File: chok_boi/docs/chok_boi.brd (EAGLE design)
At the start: 160 x 100 mm, 94 parts, among them U1 MPU-6000, U2 DRV8835

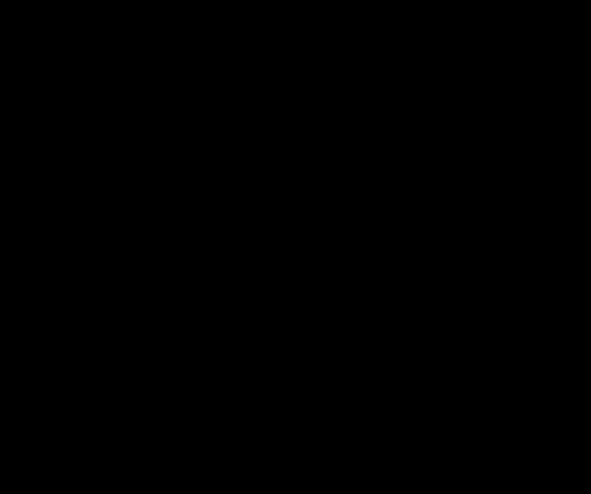
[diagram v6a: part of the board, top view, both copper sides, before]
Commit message: Add bypass caps to DRV8835
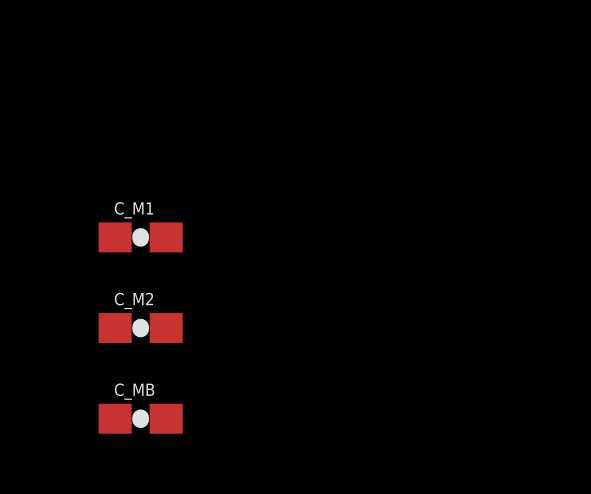
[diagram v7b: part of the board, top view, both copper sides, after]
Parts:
- added C_M1, C_M2: 0.1uF, SparkFun:0603-CAP
- added C_MB: 100uF, SparkFun:0603-CAP
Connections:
- net 3.3V: now also C_M1.2
- net BATTERY: now also C_M2.2, C_MB.2
- net MGND: now also C_M1.1, C_M2.1, C_MB.1
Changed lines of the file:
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@@
 <attribute name="PROD_ID" value="IC-13342" x="17.7038" y="37.0078" size="1.778" layer="27" display="off"/>
 </element>
+<element name="C_M1" library="SparkFun" package="0603-CAP" value="0.1uF" x="-4.5212" y="-234.3658"/>
+<element name="C_M2" library="SparkFun" package="0603-CAP" value="0.1uF" x="-4.5212" y="-237.3884"/>
+<element name="C_MB" library="SparkFun" package="0603-CAP" value="100uF" x="-4.5212" y="-240.411"/>
 </elements>
 <signals>
@@
 <wire x1="16.1846" y1="42.40075625" x2="16.1846" y2="40.9776" width="1.524" layer="1"/>
 <contactref element="U2" pad="1"/>
-<wire x1="17.1314" y1="55.3466" x2="9.906" y2="69.596" width="0" layer="19" extent="1-1"/>
-<wire x1="16.4084" y1="45.1866" x2="17.1314" y2="55.3466" width="0" layer="19" extent="1-1"/>
+<contactref element="C_M2" pad="2"/>
+<contactref element="C_MB" pad="2"/>
+<wire x1="-3.6712" y1="-237.3884" x2="-3.6712" y2="-240.411" width="0" layer="19" extent="1-1"/>
+<wire x1="16.4538" y1="35.9578" x2="-3.6712" y2="-237.3884" width="0" layer="19" extent="1-1"/>
+<wire x1="16.1846" y1="40.9776" x2="16.4538" y2="35.9578" width="0" layer="19" extent="1-1"/>
 <wire x1="6.731" y1="39.276" x2="8.57660625" y2="40.3606" width="0" layer="19" extent="1-16"/>
 <wire x1="5.461" y1="39.276" x2="6.731" y2="39.276" width="0" layer="19" extent="1-1"/>
-<wire x1="16.4538" y1="35.9578" x2="5.461" y2="39.276" width="0" layer="19" extent="1-1"/>
+<wire x1="17.1314" y1="55.3466" x2="16.4084" y2="45.1866" width="0" layer="19" extent="1-1"/>
+<wire x1="9.906" y1="69.596" x2="17.1314" y2="55.3466" width="0" layer="19" extent="1-1"/>
 </signal>
 <signal name="5V">
@@
 <wire x1="3.81" y1="27.6606" x2="3.7338" y2="27.7368" width="1.524" layer="1"/>
 <contactref element="U2" pad="12"/>
-<wire x1="2.8448" y1="11.938" x2="16.4538" y2="38.0578" width="0" layer="19" extent="1-1"/>
+<contactref element="C_M1" pad="2"/>
+<wire x1="2.8448" y1="11.938" x2="-3.6712" y2="-234.3658" width="0" layer="19" extent="1-1"/>
 <wire x1="10.0124" y1="27.5336" x2="5.908" y2="27.766" width="0" layer="19" extent="1-1"/>
 <wire x1="10.2244" y1="27.5336" x2="10.0124" y2="27.5336" width="0" layer="19" extent="1-1"/>
-<wire x1="43.6254" y1="30.9372" x2="10.2244" y2="27.5336" width="0" layer="19" extent="1-1"/>
-<wire x1="43.7016" y1="33.3502" x2="43.6254" y2="30.9372" width="0" layer="19" extent="1-1"/>
+<wire x1="16.4538" y1="38.0578" x2="10.2244" y2="27.5336" width="0" layer="19" extent="1-1"/>
+<wire x1="43.7016" y1="33.3502" x2="16.4538" y2="38.0578" width="0" layer="19" extent="1-1"/>
+<wire x1="43.6254" y1="30.9372" x2="43.7016" y2="33.3502" width="0" layer="19" extent="1-1"/>
 <wire x1="48.221" y1="33.0816" x2="43.7016" y2="33.3502" width="0" layer="19" extent="1-1"/>
 <wire x1="50.221" y1="31.0816" x2="48.221" y2="33.0816" width="0" layer="19" extent="1-1"/>
@@
 <contactref element="U2" pad="6"/>
 <contactref element="U2" pad="PAD"/>
+<contactref element="C_M1" pad="1"/>
+<contactref element="C_M2" pad="1"/>
+<contactref element="C_MB" pad="1"/>
+<wire x1="-5.3712" y1="-237.3884" x2="-5.3712" y2="-240.411" width="0" layer="19" extent="1-1"/>
+<wire x1="-5.3712" y1="-234.3658" x2="-5.3712" y2="-237.3884" width="0" layer="19" extent="1-1"/>
+<wire x1="18.9538" y1="35.9578" x2="-5.3712" y2="-234.3658" width="0" layer="19" extent="1-1"/>
 <wire x1="17.7038" y1="37.0078" x2="18.9538" y2="35.9578" width="0" layer="19" extent="1-1"/>
 <wire x1="19.939" y1="43.67940625" x2="17.7038" y2="37.0078" width="0" layer="19" extent="1-1"/>

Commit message: Add cell outline
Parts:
- moved LEFT_FRONT_EMITTER 29.6 mm to (60.0, 69.0)
- moved U$18 27.7 mm to (77.0, 42.0)
- moved REC_LF 27.2 mm to (64.0, 63.0)
- moved U$21 24.4 mm to (83.0, 47.0)
- moved U$11 11.9 mm to (67.0, 46.0), turned to 312 degrees
- moved U$17 11.9 mm to (65.0, 27.0), turned to 228 degrees
- moved U$7 10.2 mm to (66.0, 56.0)
- moved U$9 7.99 mm to (83.0, 27.0)
- moved U$13 4.82 mm to (77.2, 32.0)
- moved SERIAL2 3.00 mm to (54.0, 51.2)
- moved SERIAL1 2.00 mm to (55.0, 56.0)
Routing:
- net D2_EM: track 7.43 -> 15.1 mm
- net RF_EM: track 2.74 -> 7.56 mm
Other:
- board size 160 x 100 mm -> 372 x 192 mm
